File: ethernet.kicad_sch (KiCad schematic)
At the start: 57 parts, among them J4 Bus_RJ45_7499111121A, U9 KSZ9031RNXCA, Y1 Oscillator_SMD_25MHz_KX-7

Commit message: [#80386] Add company name in board settings
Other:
- company: Antmicro Ltd. -> Antmicro
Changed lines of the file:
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@@
 		(date "2023-07-27")
 		(rev "1.0.1")
-		(company "Antmicro Ltd.")
+		(company "Antmicro")
 		(comment 1 "www.antmicro.com")
-		(comment 2 "Antmicro Ltd")
 	)
 	(text "AVDDH decoupling"

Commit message: [#87036] Update components, clear DRC and ERC
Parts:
- removed J4: Bus_RJ45_7499111121A, data-center-rdimm-ddr5-tester-footprints:RJ45_7499111121A_Horizontal, symbol data-center-rdimm-ddr5-tester:Bus_RJ45_7499111121A
- added J9: Bus_RJ45_7499111121A, antmicro-footprints:RJ45_7499111121A_Horizontal, symbol antmicroModularConnectorsJacksWithMagnetics:Bus_RJ45_7499111121A
- C122, C125, C127, C128, C131, C133, C138: footprint data-center-rdimm-ddr5-tester-footprints:C_0402_1005Metric -> antmicro-footprints:C_0402_1005Metric; symbol data-center-rdimm-ddr5-tester:C_4u7_0402 -> antmicroCapacitors0402:C_4u7_0402
- C123, C124, C126, C130, C132, C136: footprint data-center-rdimm-ddr5-tester-footprints:C_0402_1005Metric -> antmicro-footprints:C_0402_1005Metric; symbol data-center-rdimm-ddr5-tester:C_470n_0402 -> antmicroCapacitors0402:C_470n_0402
- C134, C135, C137, C139, C140, C141, C142, C143, C144, C145: footprint data-center-rdimm-ddr5-tester-footprints:C_0402_1005Metric -> antmicro-footprints:C_0402_1005Metric; symbol data-center-rdimm-ddr5-tester:C_10n_0402 -> antmicroCapacitors0402:C_10n_0402
- C146, C147: footprint data-center-rdimm-ddr5-tester-footprints:C_0402_1005Metric -> antmicro-footprints:C_0402_1005Metric; symbol data-center-rdimm-ddr5-tester:C_22p_0402 -> antmicroCapacitors0402:C_22p_0402; Manufacturer Yaego -> YAGEO
- FB1, FB2, FB3, FB4: footprint data-center-rdimm-ddr5-tester-footprints:FB_0603_1608Metric -> antmicro-footprints:FB_0603_1608Metric; symbol data-center-rdimm-ddr5-tester:FB_120Z_2A_0603 -> antmicroFerriteBeadsandChips:FB_120Z_2A_Murata-BLM18PG_0603; Val (none) -> 120Z/2A
- R58, R60: footprint data-center-rdimm-ddr5-tester-footprints:R_0402_1005Metric -> antmicro-footprints:R_0402_1005Metric; symbol data-center-rdimm-ddr5-tester:R_220R_0402 -> antmicroResistors0402:R_220R_0402
- R59: footprint data-center-rdimm-ddr5-tester-footprints:R_0402_1005Metric -> antmicro-footprints:R_0402_1005Metric; symbol data-center-rdimm-ddr5-tester:R_12k1_0402 -> antmicroResistors0402:R_12k1_0402
- R61: footprint data-center-rdimm-ddr5-tester-footprints:R_0402_1005Metric -> antmicro-footprints:R_0402_1005Metric; symbol data-center-rdimm-ddr5-tester:R_1M8_0402 -> antmicroResistors0402:R_1M8_5%_0402; MPN CR0402-FX-1804GLF -> MCMR04X185_JTL; Manufacturer Bourns -> Multicomp Pro; Tolerance 1% -> 5%
- R62, R63, R66, R67: footprint data-center-rdimm-ddr5-tester-footprints:R_0402_1005Metric -> antmicro-footprints:R_0402_1005Metric; symbol data-center-rdimm-ddr5-tester:R_10k2_0402 -> antmicroResistors0402:R_10k2_0402; DNP DNP -> (none); now not fitted; now left out of the parts list
- R64, R65, R68, R69, R70, R72: footprint data-center-rdimm-ddr5-tester-footprints:R_0402_1005Metric -> antmicro-footprints:R_0402_1005Metric; symbol data-center-rdimm-ddr5-tester:R_10k2_0402 -> antmicroResistors0402:R_10k2_0402
- R71: footprint data-center-rdimm-ddr5-tester-footprints:R_0402_1005Metric -> antmicro-footprints:R_0402_1005Metric; symbol data-center-rdimm-ddr5-tester:R_1k_0402 -> antmicroResistors0402:R_1k_0402
- R73, R74, R77, R78: footprint data-center-rdimm-ddr5-tester-footprints:R_0402_1005Metric -> antmicro-footprints:R_0402_1005Metric; symbol data-center-rdimm-ddr5-tester:R_2k2_0402 -> antmicroResistors0402:R_2k2_0402
- R75, R76, R79, R80, R81: footprint data-center-rdimm-ddr5-tester-footprints:R_0402_1005Metric -> antmicro-footprints:R_0402_1005Metric; symbol data-center-rdimm-ddr5-tester:R_2k2_0402 -> antmicroResistors0402:R_2k2_0402; DNP DNP -> (none); now not fitted; now left out of the parts list
- U9: footprint data-center-rdimm-ddr5-tester-footprints:QFN-48-1EP_7x7x0.9mm_P0.5mm_EP3.5x3.5mm -> antmicro-footprints:QFN-48-1EP_7x7x0.9mm_P0.5mm_EP3.5x3.5mm; symbol data-center-rdimm-ddr5-tester:KSZ9031RNXCA -> antmicroInterfaceControllers:KSZ9031RNXCA; Manufacturer Microchip -> Microchip Technology
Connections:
- net ETH1_N: now also J9.2 (D1-)
- net ETH1_P: now also J9.1 (D1+)
- net ETH2_N: now also J9.6 (D2-)
- net ETH2_P: now also J9.3 (D2+)
- net ETH3_N: now also J9.5 (D3-)
- net ETH3_P: now also J9.4 (D3+)
- net ETH4_N: now also J9.8 (D4-)
- net ETH4_P: now also J9.7 (D4+)
- net GND: now also J9.10 (GND)
- net LED_LINK: now also J9.12 (LED1_Y-)
- net LED_SPD: now also J9.14 (LED2_G-)
- net at U9.13 (NC): no longer U9.47 (NC)
- net at R58.1: now also J9.11 (LED1_Y+)
- net at R60.1: now also J9.13 (LED2_G+)
- net at FB4.1: now also J9.SH
- net 1V2_SYS renamed +1V2
- net 3V3_SYS renamed +3V3
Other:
- moved on the sheet: C122, C123, C124, C125, C126, C127, C128, C130, C132, C133, C134, C135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

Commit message: [#87036] Update R61
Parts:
- R61: symbol antmicroResistors0402:R_1M8_5%_0402 -> antmicroResistors0402:R_1M8_0402; MPN MCMR04X185_JTL -> RC0402FR-071M8L; Manufacturer Multicomp Pro -> YAGEO; Tolerance 5% -> 1%
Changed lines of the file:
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@@
 	)
 	(symbol
-		(lib_id "antmicroResistors0402:R_1M8_5%_0402")
+		(lib_id "antmicroResistors0402:R_1M8_0402")
 		(at 194.31 116.84 0)
 		(mirror y)
@@
 			)
 		)
-		(property "Datasheet" "https://www.farnell.com/datasheets/2860635.pdf"
+		(property "Datasheet" "https://www.mouser.com/catalog/specsheets/YAGEO_PYu_RC_Group_51_RoHS_L_12.pdf"
 			(at 173.99 134.62 0)
 			(effects
@@
 			)
 		)
-		(property "Description" "SMD Chip Resistor, Ceramic, 1.8 Mohm, ± 5%, 62.5 mW, 0402 [1005 Metric], Thick Film"
+		(property "Description" "SMD Chip Resistor"
 			(at 173.99 147.32 0)
 			(effects
@@
 			)
 		)
-		(property "Manufacturer" "Multicomp Pro"
+		(property "Manufacturer" "YAGEO"
 			(at 173.99 139.7 0)
 			(effects
@@
 			)
 		)
-		(property "MPN" "MCMR04X185_JTL"
+		(property "MPN" "RC0402FR-071M8L"
 			(at 173.99 137.16 0)
 			(effects
@@
 		)
 		(property "Val" "1M8"
-			(at 196.342 115.57 0)
+			(at 198.12 116.332 0)
 			(effects
 				(font
@@
 					(thickness 0.15)
 				)
+				(justify left bottom)
 			)
 		)
@@
 			)
 		)
-		(property "Tolerance" "5%"
+		(property "Tolerance" "1%"
 			(at 173.99 127 0)
 			(effects

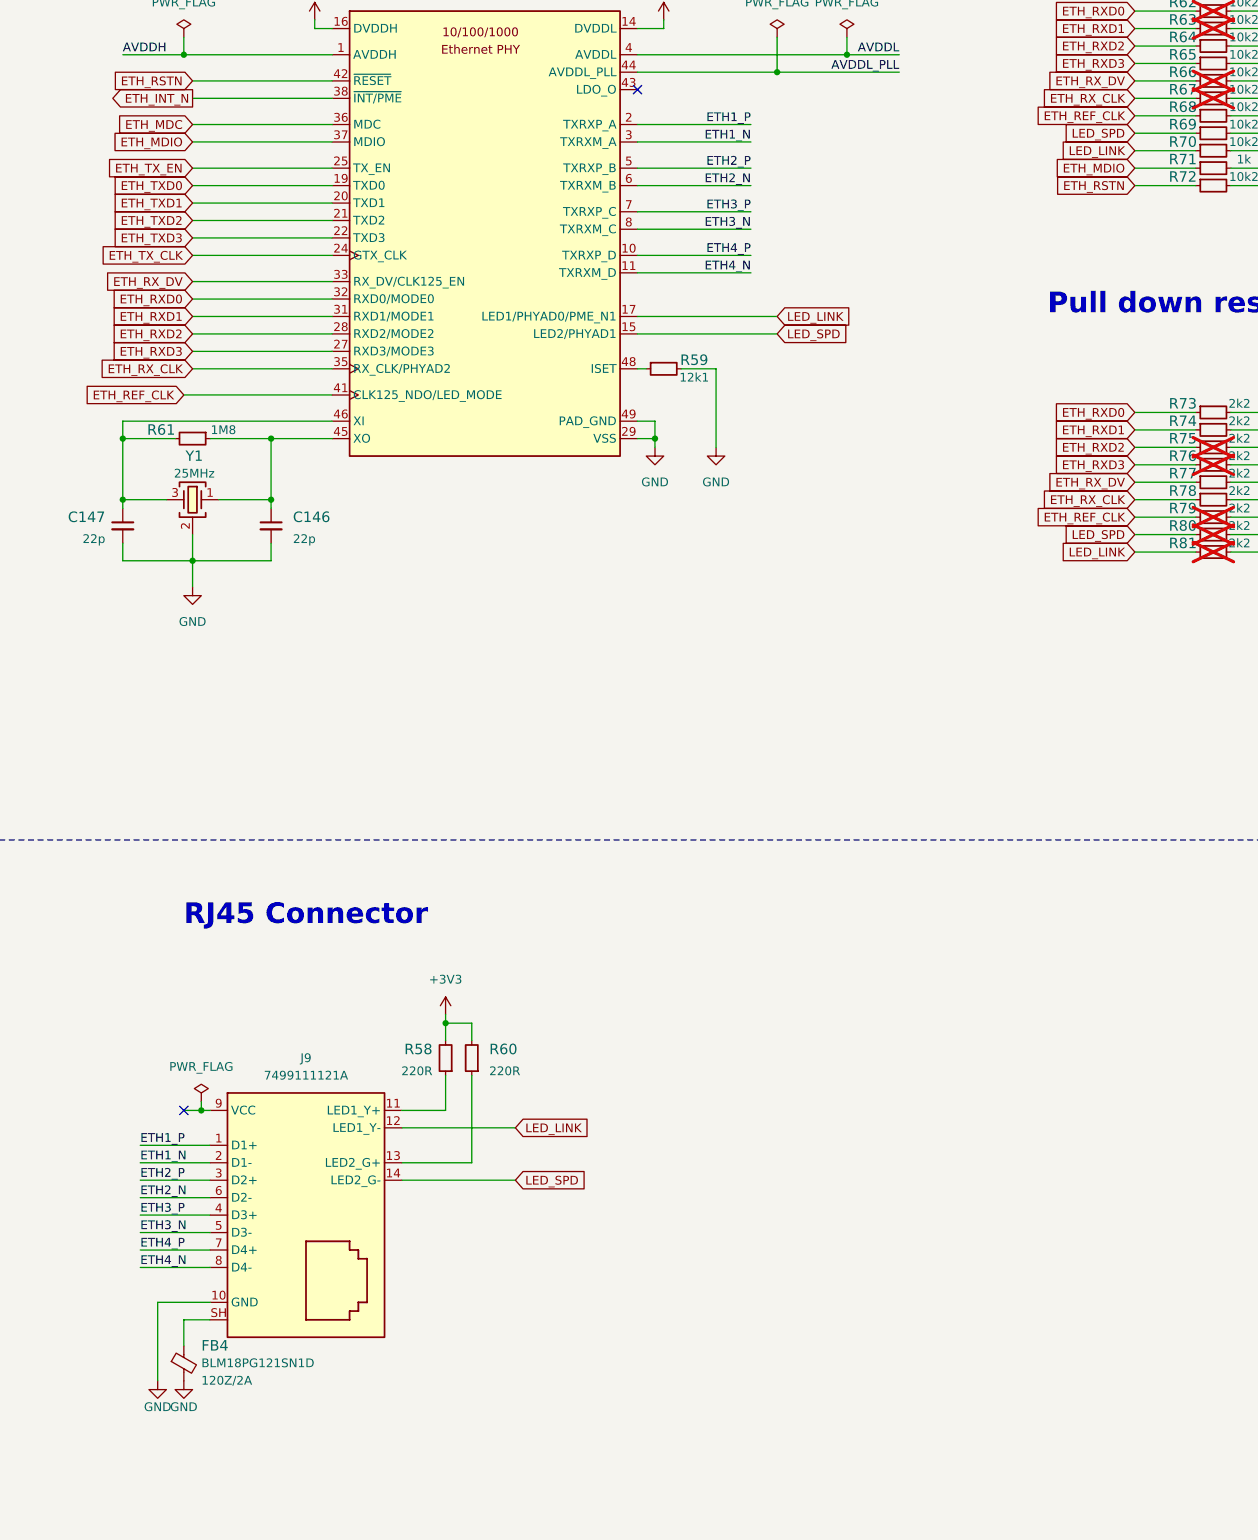
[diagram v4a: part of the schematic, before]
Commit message: [#87036] Replace RJ45 connector
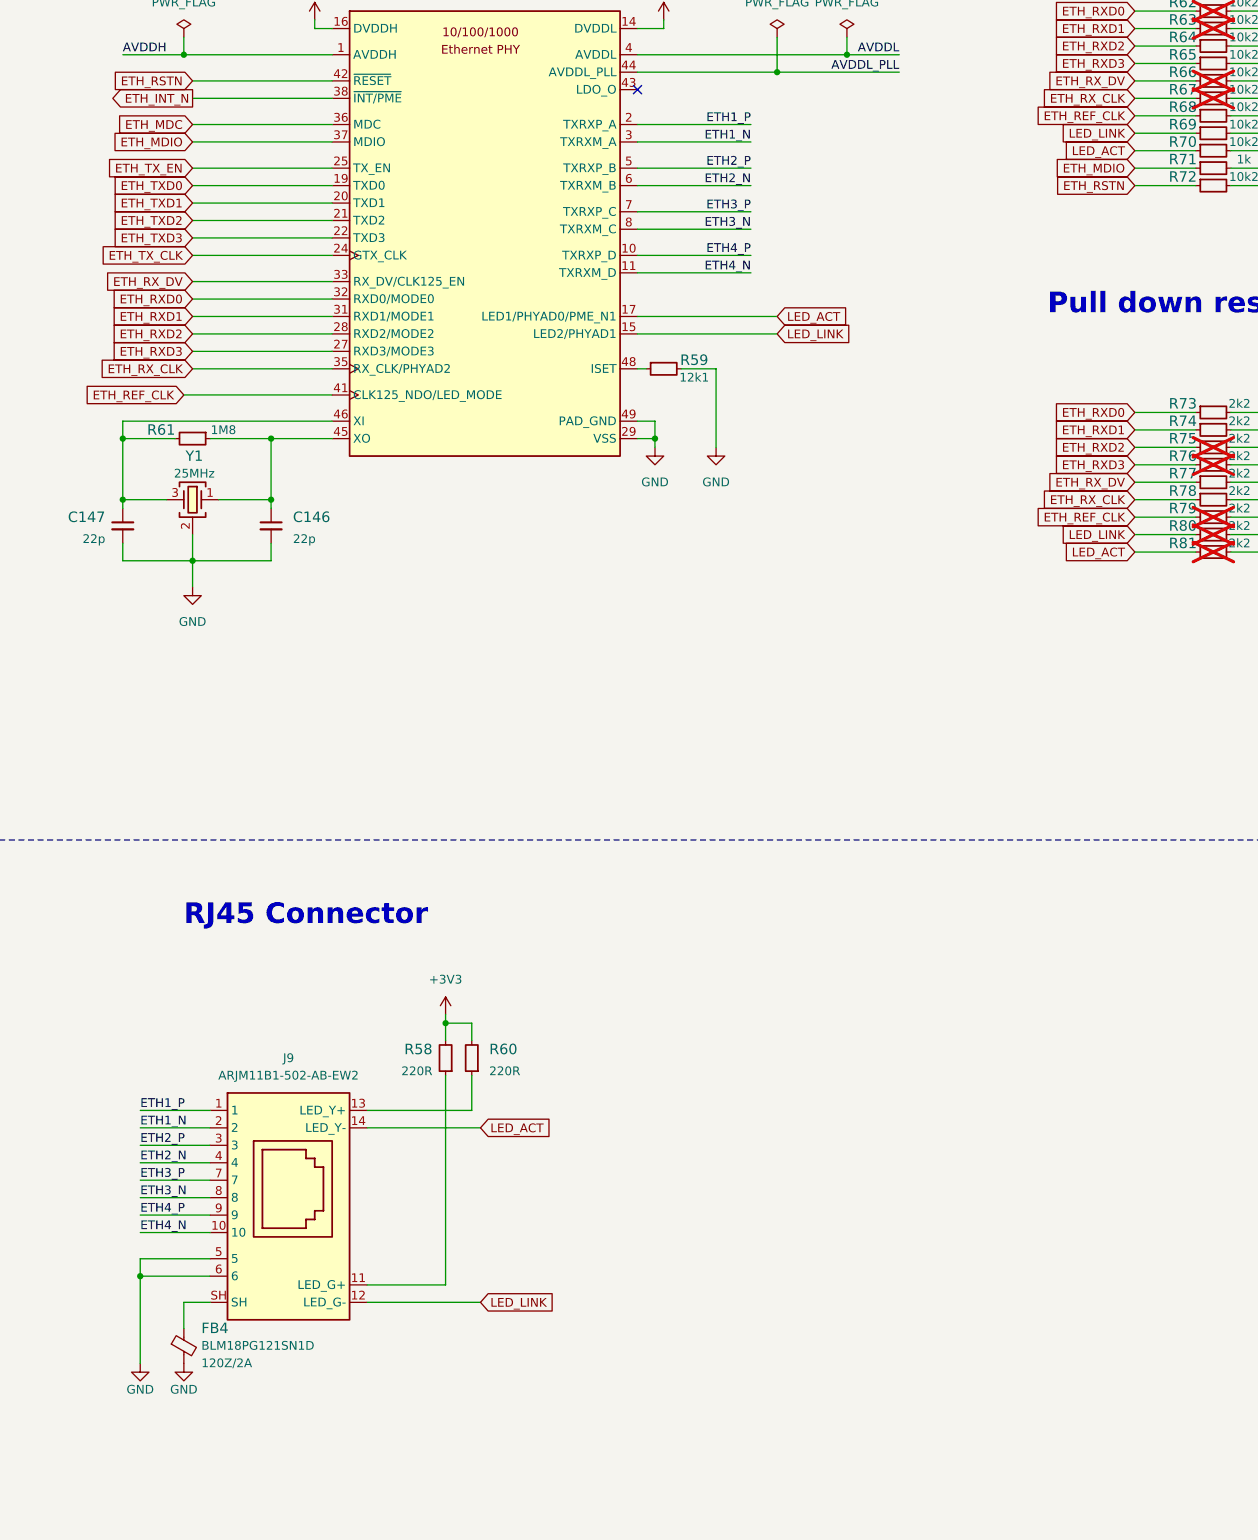
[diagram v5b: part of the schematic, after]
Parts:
- J9: footprint antmicro-footprints:RJ45_7499111121A_Horizontal -> antmicro-footprints:RJ45_ARJM11B1-502-AB-EW2_Horizontal; symbol antmicroModularConnectorsJacksWithMagnetics:Bus_RJ45_7499111121A -> antmicroModularConnectorsJacks:RJ45_Abracon_ARJM11B1-502-AB-EW2; MPN 7499111121A -> ARJM11B1-502-AB-EW2; Manufacturer Würth Elektronik -> Abracon
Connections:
- net ETH2_N: now also J9.4; no longer J9.6 (D2-)
- net ETH3_N: now also J9.8; no longer J9.5 (D3-)
- net ETH3_P: now also J9.7; no longer J9.4 (D3+)
- net ETH4_N: now also J9.10; no longer J9.8 (D4-)
- net ETH4_P: now also J9.9; no longer J9.7 (D4+)
- net GND: now also J9.5, J9.6; no longer J9.10 (GND)
- net LED_LINK: now also R69.1, R80.1, U9.15 (LED2/PHYAD1); no longer R70.1, R81.1, U9.17 (LED1/PHYAD0/PME_N1)
- removed net LED_SPD: J9.14 (LED2_G-), R69.1, R80.1, U9.15 (LED2/PHYAD1)
- new net LED_ACT: J9.14 (LED_Y-), R70.1, R81.1, U9.17 (LED1/PHYAD0/PME_N1)
- no-connect marks 2 -> 1
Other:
- moved on the sheet: FB4

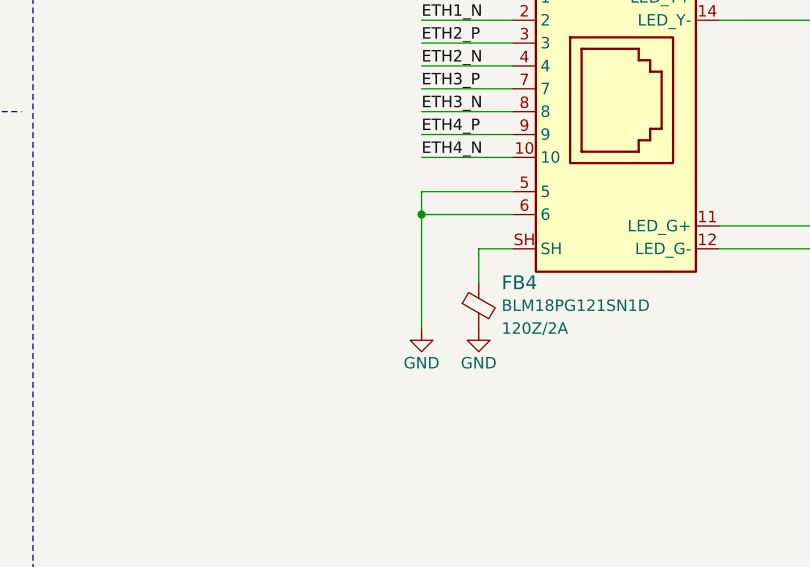
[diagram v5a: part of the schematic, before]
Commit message: [#87036] Fix RJ45 GND connection
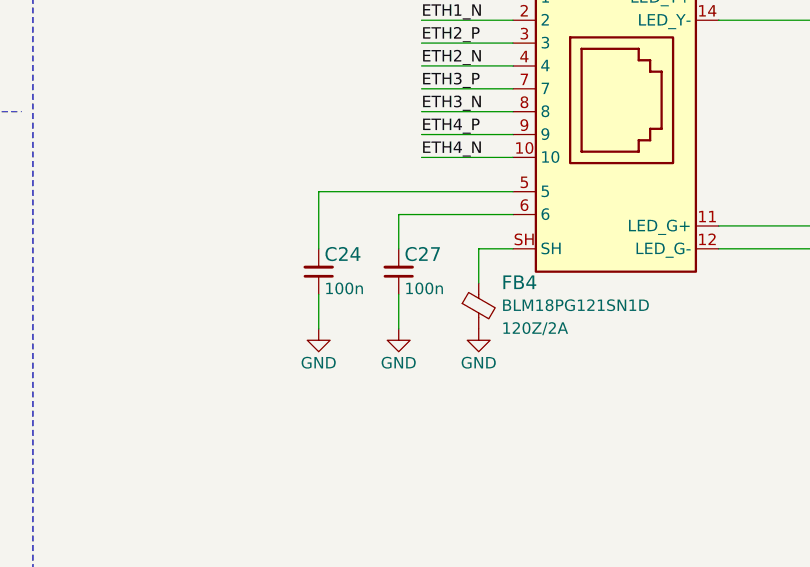
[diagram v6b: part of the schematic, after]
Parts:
- added C24, C27: C_100n_16V_0402, data-center-rdimm-ddr5-tester-footprints:C_0402_1005Metric, symbol data-center-rdimm-ddr5-tester:C_100n_16V_0402
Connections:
- net GND: now also C24.1, C27.1; no longer J9.5, J9.6
- new net: C27.2, J9.6
- new net: C24.2, J9.5
